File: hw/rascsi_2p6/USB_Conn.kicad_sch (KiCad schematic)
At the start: 4 parts, among them J8 USB_B_Micro

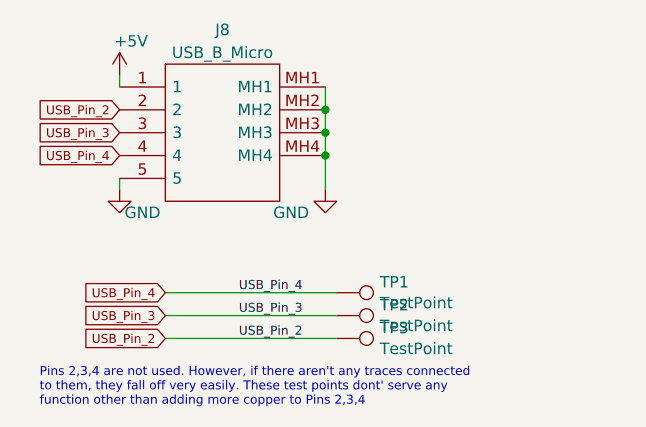
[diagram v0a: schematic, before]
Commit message: Updated with 74LVT245 - as ordered
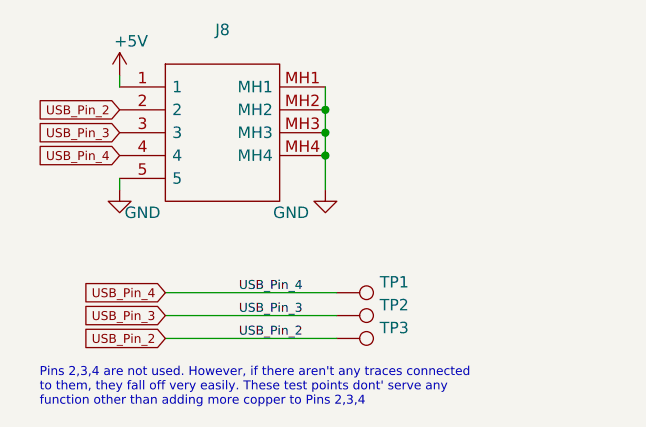
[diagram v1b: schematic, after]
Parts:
- J8: value USB_B_Micro -> (none); footprint SamacSys_Parts:U254051N4BH806 -> (none)
- TP1, TP2, TP3: value TestPoint -> (none); footprint TestPoint:TestPoint_Pad_D1.0mm -> (none)
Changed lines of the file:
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@@
     (in_bom yes) (on_board yes)
     (property "Reference" "J8" (id 0) (at 85.09 45.72 0))
-    (property "Value" "USB_B_Micro" (id 1) (at 85.09 48.26 0))
-    (property "Footprint" "SamacSys_Parts:U254051N4BH806" (id 2) (at 77.47 53.34 0)
+    (property "Value" "" (id 1) (at 85.09 48.26 0))
+    (property "Footprint" "" (id 2) (at 77.47 53.34 0)
       (effects (font (size 1.27 1.27)) hide)
     )
@@
       (effects (font (size 1.27 1.27)) (justify left))
     )
-    (property "Value" "TestPoint" (id 1) (at 102.5652 76.073 90)
+    (property "Value" "" (id 1) (at 102.5652 76.073 90)
       (effects (font (size 1.27 1.27)) (justify left))
     )
-    (property "Footprint" "TestPoint:TestPoint_Pad_D1.0mm" (id 2) (at 97.79 80.01 0)
+    (property "Footprint" "" (id 2) (at 97.79 80.01 0)
       (effects (font (size 1.27 1.27)) hide)
     )
@@
       (effects (font (size 1.27 1.27)) (justify left))
     )
-    (property "Value" "TestPoint" (id 1) (at 102.5652 78.613 90)
+    (property "Value" "" (id 1) (at 102.5652 78.613 90)
       (effects (font (size 1.27 1.27)) (justify left))
     )
-    (property "Footprint" "TestPoint:TestPoint_Pad_D1.0mm" (id 2) (at 97.79 82.55 0)
+    (property "Footprint" "" (id 2) (at 97.79 82.55 0)
       (effects (font (size 1.27 1.27)) hide)
     )
@@
       (effects (font (size 1.27 1.27)) (justify left))
     )
-    (property "Value" "TestPoint" (id 1) (at 102.5652 81.153 90)
+    (property "Value" "" (id 1) (at 102.5652 81.153 90)
       (effects (font (size 1.27 1.27)) (justify left))
     )
-    (property "Footprint" "TestPoint:TestPoint_Pad_D1.0mm" (id 2) (at 97.79 85.09 0)
+    (property "Footprint" "" (id 2) (at 97.79 85.09 0)
       (effects (font (size 1.27 1.27)) hide)
     )
